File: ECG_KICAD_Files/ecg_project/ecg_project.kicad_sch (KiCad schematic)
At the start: 0 parts

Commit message: schematic update
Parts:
- added C1, C2, C3, C4, C5, C6, C7: C, symbol Device:C
- added R1, R10, R11, R12, R13, R2, R3, R4, R5, R6, R7, R8, R9: R, symbol Device:R
- added U1: LF412ACN/NOPB, N08E, symbol 2026-02-26_19-36-44:LF412ACN_NOPB
- added U2: AD623AN, symbol Amplifier_Instrumentation:AD623AN
- added U3: LF412ACN/NOPB, N08E, symbol 2026-02-26_19-47-40:LF412ACN_NOPB
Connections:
- new net: R1.2, U2.2 (-)
- new net: C1.2, R4.2, U1.3 (IN+)
- new net: C7.2, R11.1
- new net: R11.2, R12.1
- new net: C4.2, R5.1, U1.1 (OUT), U1.2 (IN-)
- new net: C2.1, C3.1, R5.2, R6.1
- new net: C2.2, C3.2
- new net: C6.1, R10.1
- new net: C6.2, R10.2
- new net: R12.2, U3.6 (IN-)
- new net: C1.1, U2.6
- new net: C5.1, R6.2, U1.5 (IN+)
- new net: C4.1, C5.2, R7.2, R8.2
- new net: R9.1, U1.6 (IN-), U1.7 (OUT)
- new net: R9.2, U3.2 (IN-)
- new net: R3.1, U2.8 (Rg)
- new net: R3.2, U2.1 (Rg)
- new net: C7.1, U3.1 (OUT)
- new net: R7.1, R8.1
- new net: R2.2, U2.3 (+)

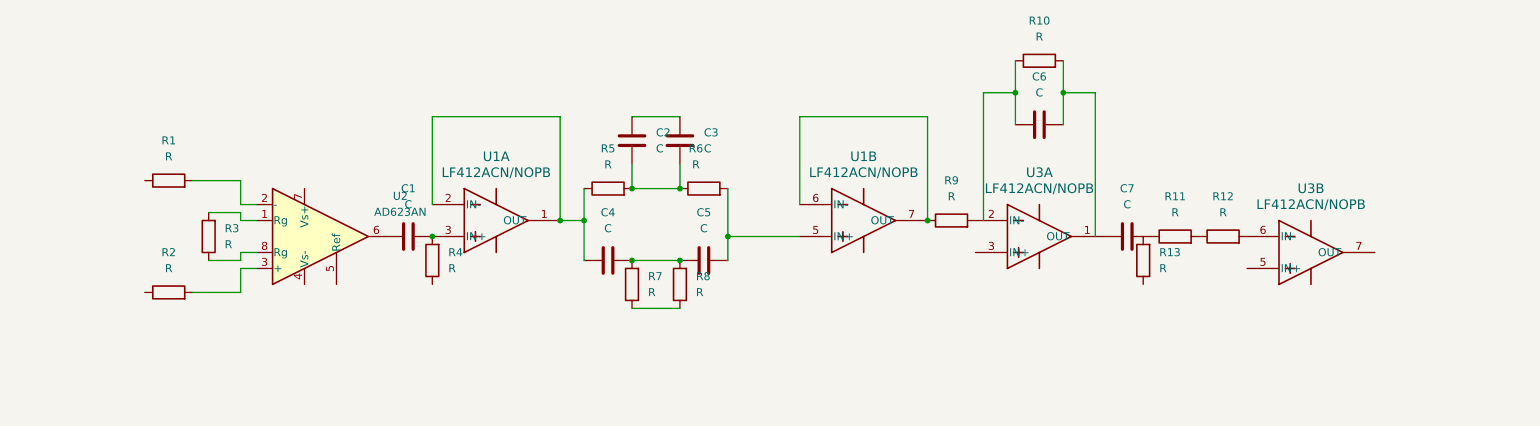
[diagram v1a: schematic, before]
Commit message: schematic update
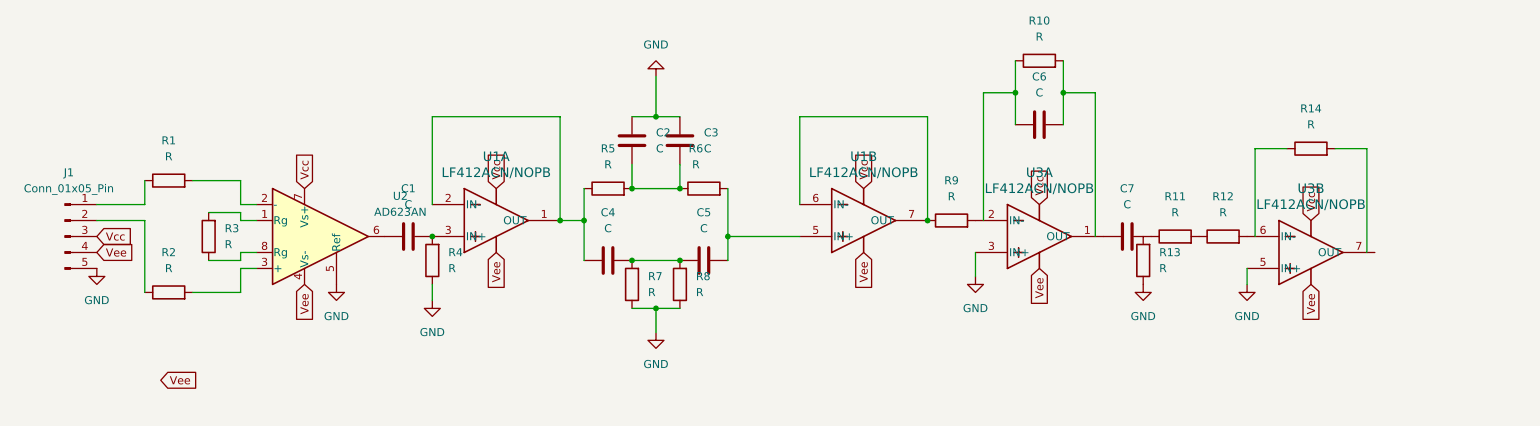
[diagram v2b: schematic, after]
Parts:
- added J1: Conn_01x05_Pin, symbol Connector:Conn_01x05_Pin
- added R14: R, symbol Device:R
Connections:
- net at R1.1: now also J1.1 (Pin_1)
- net GND: now reaches R4.1
- net GND: now also C2.2, C3.2, R13.1, R7.1, R8.1, U2.5 (Ref), U3.3 (IN+), U3.5 (IN+), J1.5 (Pin_5)
- net at R2.1: now also J1.2 (Pin_2)
- net Vee: now reaches U2.4 (Vs-)
- net Vee: now also J1.4 (Pin_4)
- net Vcc: now reaches U2.7 (Vs+)
- net Vcc: now also J1.3 (Pin_3)

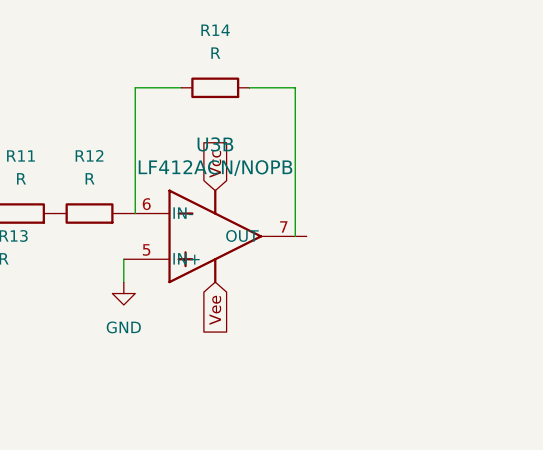
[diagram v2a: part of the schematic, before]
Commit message: schematic update
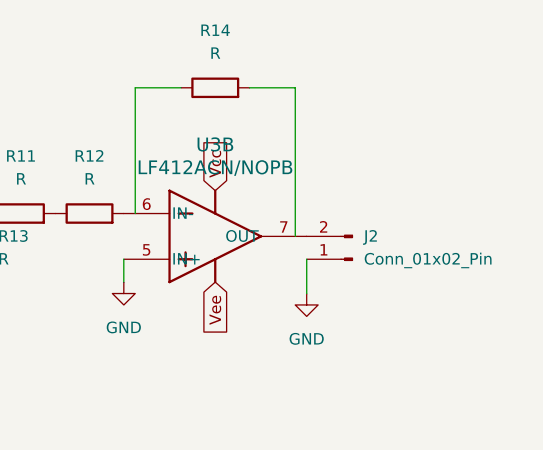
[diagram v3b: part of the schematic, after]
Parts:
- added J2: Conn_01x02_Pin, symbol Connector:Conn_01x02_Pin
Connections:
- net GND: now also J2.1 (Pin_1)
- net at U3.7 (OUT): now also J2.2 (Pin_2)
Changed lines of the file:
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@@
+	(wire
+		(pts
+			(xy 224.79 57.15) (xy 224.79 60.96)
+		)
+		(stroke
+			(width 0)
+			(type default)
+		)
+	)
 	(wire
 		(pts
@@
 	)
 	(symbol
+		(lib_id "power:GND")
+		(at 224.79 60.96 0)
+		(unit 1)
+		(exclude_from_sim no)
+		(in_bom yes)
+		(on_board yes)
+		(dnp no)
+		(fields_autoplaced yes)
+		(property "Reference" "#PWR09"
+			(at 224.79 67.31 0)
+			(effects
+				(font
+					(size 1.27 1.27)
+				)
+				(hide yes)
+			)
+		)
+		(property "Value" "GND"
+			(at 224.79 66.04 0)
+			(effects
+				(font
+					(size 1.27 1.27)
+				)
+			)
+		)
+		(property "Footprint" ""
+			(at 224.79 60.96 0)
+			(effects
+				(font
+					(size 1.27 1.27)
+				)
+				(hide yes)
+			)
+		)
+		(property "Datasheet" ""
+			(at 224.79 60.96 0)
+			(effects
+				(font
+					(size 1.27 1.27)
+				)
+				(hide yes)
+			)
+		)
+		(property "Description" "Power symbol creates a global label with name \"GND\" , ground"
+			(at 224.79 60.96 0)
+			(effects
+				(font
+					(size 1.27 1.27)
+				)
+				(hide yes)
+			)
+		)
+		(pin "1"
+		)
+		(instances
+			(project ""
+				(path "/5671ef2c-0bd4-4b4b-87fa-f25d1993f772"
+					(reference "#PWR09")
+					(unit 1)
+				)
+			)
+		)
+	)
+	(symbol
 		(lib_id "2026-02-26_19-36-44:LF412ACN_NOPB")
 		(at 80.01 44.45 0)
@@
 				)
 			)
+		)
+	)
+	(symbol
+		(lib_id "Connector:Conn_01x02_Pin")
+		(at 229.87 57.15 180)
+		(unit 1)
+		(exclude_from_sim no)
+		(in_bom yes)
+		(on_board yes)
+		(dnp no)
+		(fields_autoplaced yes)
+		(property "Reference" "J2"
+			(at 231.14 54.6099 0)
+			(effects
+				(font
+					(size 1.27 1.27)
+				)
+				(justify right)
+			)
+		)
+		(property "Value" "Conn_01x02_Pin"
+			(at 231.14 57.1499 0)
+			(effects
+				(font
+					(size 1.27 1.27)
+				)
+				(justify right)
+			)
+		)
+		(property "Footprint" ""
+			(at 229.87 57.15 0)
+			(effects
+				(font
+					(size 1.27 1.27)
+				)
+				(hide yes)
+			)
+		)
+		(property "Datasheet" "~"
+			(at 229.87 57.15 0)
+			(effects
+				(font
+					(size 1.27 1.27)
+				)
+				(hide yes)
+			)
+		)
+		(property "Description" "Generic connector, single row, 01x02, script generated"
+			(at 229.87 57.15 0)
+			(effects
+				(font
+					(size 1.27 1.27)
+				)
+				(hide yes)
+			)
+		)
+		(pin "2"
+		)
+		(pin "1"
+		)
+		(instances
+			(project ""
+				(path "/5671ef2c-0bd4-4b4b-87fa-f25d1993f772"
+					(reference "J2")
+					(unit 1)
+				)
+			)

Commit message: update
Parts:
- removed J1: Conn_01x05_Pin, symbol Connector:Conn_01x05_Pin
- added J1: Conn_01x02_Pin, Connector_PinHeader_2.54mm:PinHeader_1x02_P2.54mm_Horizontal, symbol Connector:Conn_01x02_Pin
- added J3: Conn_01x03_Pin, Connector_PinHeader_2.54mm:PinHeader_1x03_P2.54mm_Horizontal, symbol Connector:Conn_01x03_Pin
- added R15, R16: R, Resistor_THT:R_Axial_DIN0204_L3.6mm_D1.6mm_P7.62mm_Horizontal, symbol Device:R
- C1, C2, C3, C4, C5, C6, C7: footprint (none) -> Capacitor_THT:C_Axial_L3.8mm_D2.6mm_P7.50mm_Horizontal
- J2: footprint (none) -> Connector_PinHeader_2.54mm:PinHeader_1x02_P2.54mm_Horizontal
- R1, R10, R11, R12, R13, R14, R2, R3, R4, R5, R6, R7, R8, R9: footprint (none) -> Resistor_THT:R_Axial_DIN0204_L3.6mm_D1.6mm_P7.62mm_Horizontal
- U2: footprint (none) -> Package_DIP:DIP-8_W7.62mm
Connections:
- net GND: now also J3.1 (Pin_1), R15.1; no longer U3.5 (IN+)
- net Vcc: now also J3.2 (Pin_2), R16.1
- net Vee: now also J3.3 (Pin_3)
- net at R1.1: now also J1.1 (Pin_1)
- net at R2.1: now also J1.2 (Pin_2)
- new net: R15.2, R16.2, U3.5 (IN+)
